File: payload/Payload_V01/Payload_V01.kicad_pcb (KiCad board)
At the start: 2 copper layers, 90.2 x 95.9 mm, 36 parts, among them J1 Screw_Terminal_01x02, J2 Screw_Terminal_01x02, J3 Conn_Coaxial, J4 Conn_Coaxial, J5 Conn_Coaxial, U2 AD9838, U4 STM32F407VETx

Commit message: created payload cutout and exported
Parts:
- moved C10 39.0 mm to (187.0, 57.5), turned to 90 degrees
- moved R4 37.9 mm to (186.9, 53.4), turned to 90 degrees
- moved U2 27.2 mm to (154.3, 128.7)
- moved R1 27.0 mm to (183.1, 57.5), turned to 90 degrees
- moved C18 24.3 mm to (170.8, 64.6), turned to 90 degrees
- moved R2 23.0 mm to (164.0, 53.2), turned to 90 degrees
- moved C5 20.7 mm to (175.9, 65.2), turned to 90 degrees
- moved C14 20.6 mm to (164.0, 57.6), turned to 90 degrees
- moved D1 20.1 mm to (178.2, 92.1)
- moved C6 17.6 mm to (179.6, 65.1), turned to 90 degrees
- moved C7 16.2 mm to (159.8, 52.4)
- moved C12 16.2 mm to (159.8, 55.0)
- moved C16 16.2 mm to (159.8, 57.5)
- moved U4 15.7 mm to (134.1, 129.4)
- moved C15 15.6 mm to (179.5, 57.7), turned to 90 degrees
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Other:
- outline, holes or cut-outs redrawn

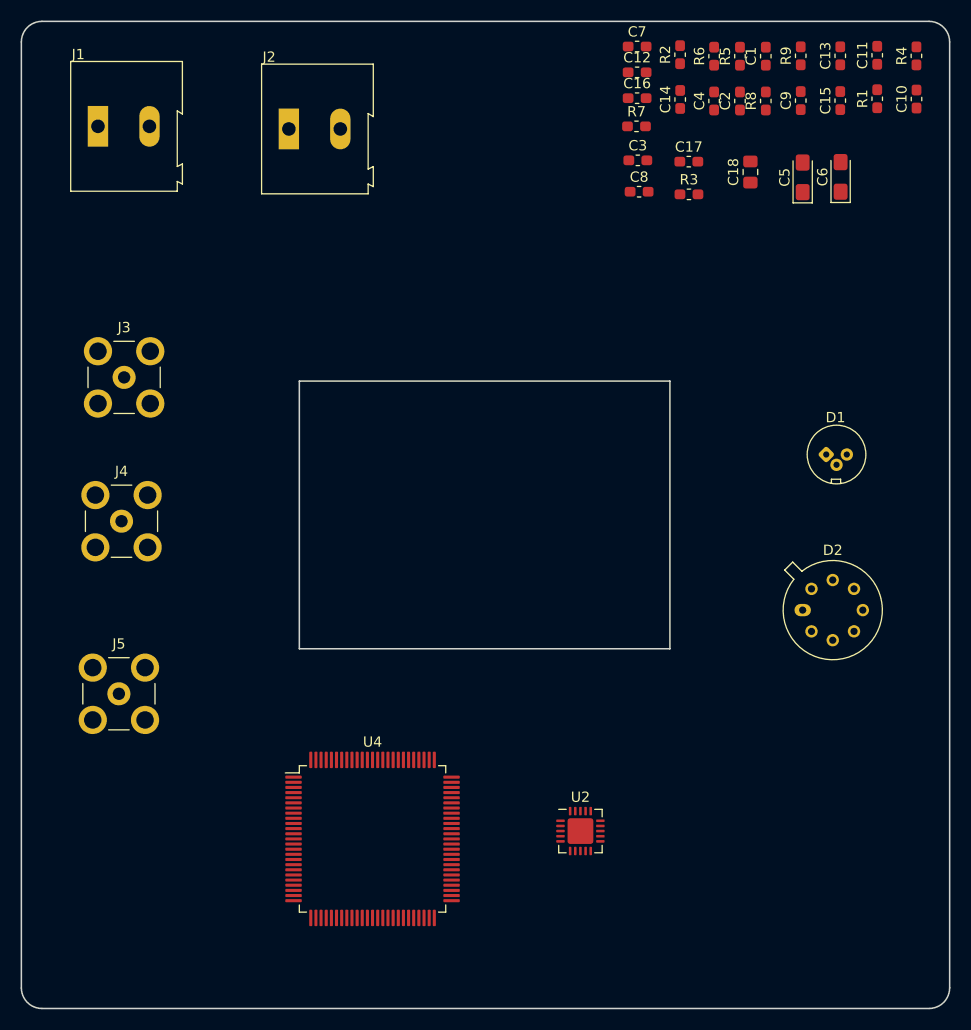
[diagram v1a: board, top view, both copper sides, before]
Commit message: added footprints and 3d models
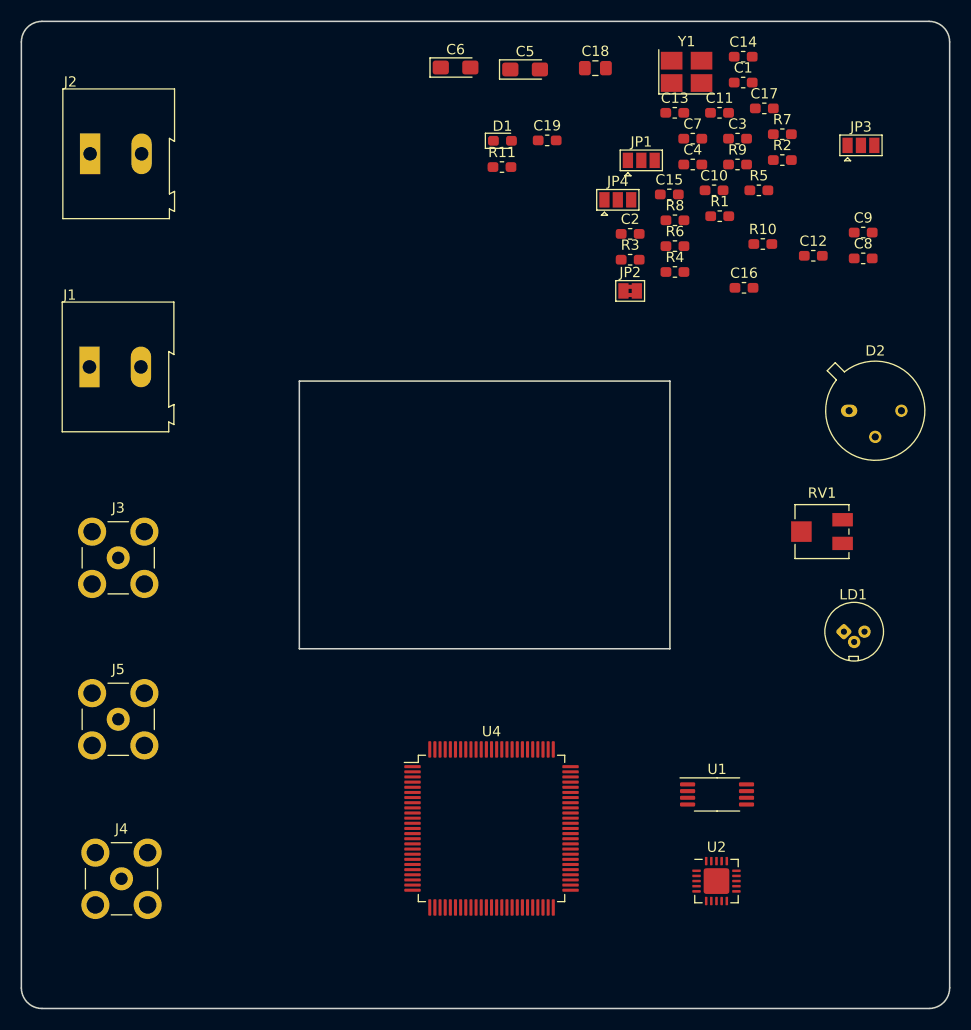
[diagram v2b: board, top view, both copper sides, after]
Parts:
- added C19: C, Resistor_SMD:R_0603_1608Metric_Pad1.05x0.95mm_HandSolder, F.Cu at (151.1, 61.6)
- added JP1: Jumper_3_Open, Jumper:SolderJumper-3_P1.3mm_Open_Pad1.0x1.5mm, F.Cu at (160.2, 63.5)
- added JP2: Jumper, Jumper:SolderJumper-2_P1.3mm_Bridged2Bar_Pad1.0x1.5mm, F.Cu at (159.1, 76.2)
- added JP3: Jumper_3_Open, Jumper:SolderJumper-3_P1.3mm_Open_Pad1.0x1.5mm, F.Cu at (181.6, 62.0)
- added JP4: Jumper_3_Open, Jumper:SolderJumper-3_P1.3mm_Open_Pad1.0x1.5mm, F.Cu at (157.9, 67.3)
- added LD1: DJ532-40, OptoDevice:LaserDiode_TO18-D5.6-3, F.Cu at (179.9, 109.3)
- added R10: 1k, Resistor_SMD:R_0603_1608Metric_Pad1.05x0.95mm_HandSolder, F.Cu at (172.0, 71.6)
- added R11: R_US, Resistor_SMD:R_0603_1608Metric_Pad1.05x0.95mm_HandSolder, F.Cu at (146.7, 64.2)
- added RV1: 10k, Potentiometer_SMD:Potentiometer_Vishay_TS53YJ_Vertical, F.Cu at (177.8, 99.6)
- added U1: REF196, Package_SO:TSSOP-8_4.4x3mm_P0.65mm, F.Cu at (167.6, 125.1)
- added Y1: SG-310SCF, Crystal:Crystal_SMD_SeikoEpson_TSX3225-4Pin_3.2x2.5mm_HandSoldering, F.Cu at (164.6, 54.9)
- D1: footprint OptoDevice:LaserDiode_TO18-D5.6-3 -> Diode_SMD:D_0603_1608Metric_Pad1.05x0.95mm_HandSolder
- D2: footprint Package_TO_SOT_THT:TO-5-8 -> Package_TO_SOT_THT:TO-5-3
- moved D1 43.8 mm to (146.7, 61.6)
- moved C6 38.9 mm to (142.2, 54.5), turned to 0 degrees
- moved J4 34.7 mm to (109.7, 133.3)
- moved R4 31.5 mm to (163.5, 74.3), turned to 0 degrees
- moved C5 28.9 mm to (148.9, 54.7), turned to 0 degrees
- moved C12 24.7 mm to (176.9, 72.8)
- moved J1 23.4 mm to (106.6, 83.6)
- moved C8 22.7 mm to (181.8, 73.0)
- moved C10 21.6 mm to (167.3, 66.4), turned to 0 degrees
- moved C16 21.1 mm to (170.2, 75.9)
- moved D2 19.9 mm to (180.4, 87.8)
- moved J2 19.5 mm to (106.7, 62.9)
- moved R1 19.1 mm to (167.8, 68.9), turned to 0 degrees
- moved C15 18.9 mm to (162.9, 66.8), turned to 0 degrees
- moved R6 18.8 mm to (163.5, 71.8), turned to 0 degrees
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
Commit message: added driver footprint and model
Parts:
- added U3: MLD203CLN, Payload_V01:MLD203CLN, F.Cu at (133.7, 72.8)

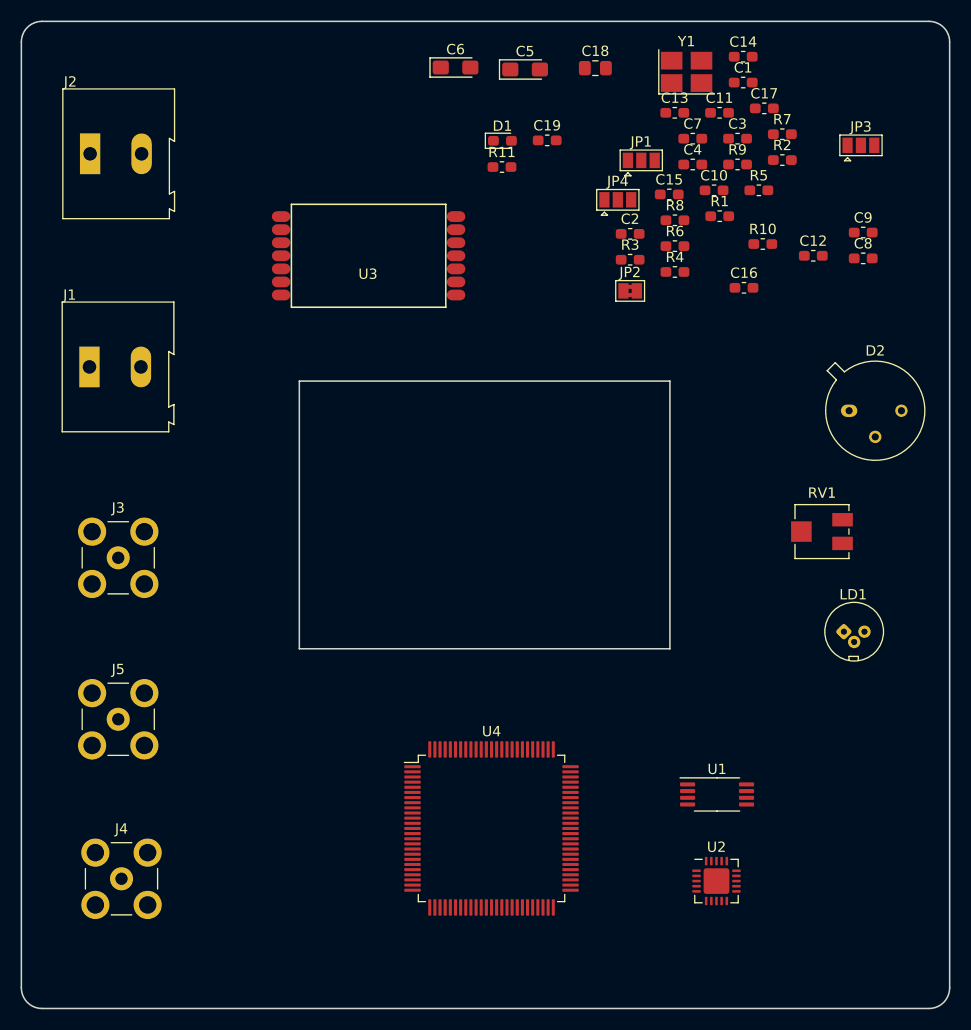
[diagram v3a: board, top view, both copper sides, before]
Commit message: fixed op amp footprint
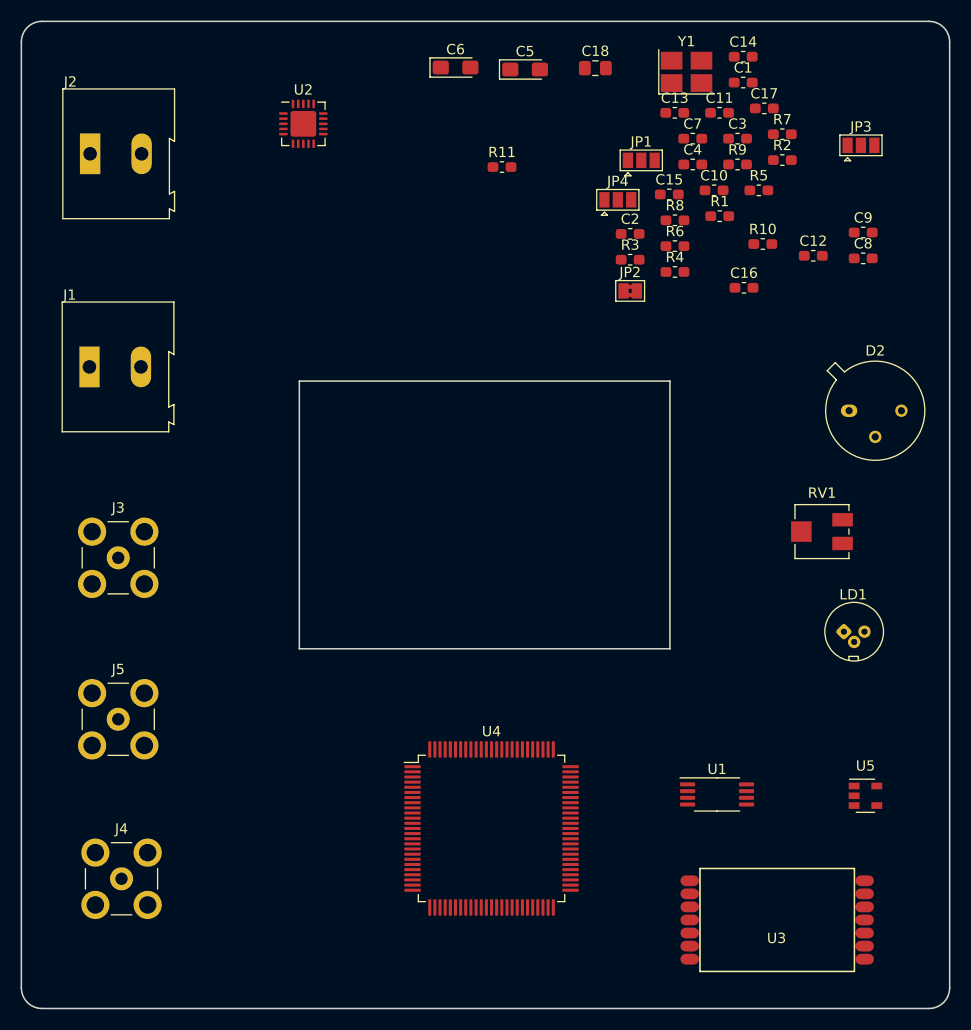
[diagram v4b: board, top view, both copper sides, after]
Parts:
- removed C19: C, Resistor_SMD:R_0603_1608Metric_Pad1.05x0.95mm_HandSolder
- removed D1: D, Diode_SMD:D_0603_1608Metric_Pad1.05x0.95mm_HandSolder
- added U5: LM321, Package_TO_SOT_SMD:SOT-23-5, F.Cu at (182.0, 125.2)
- moved U2 83.8 mm to (127.4, 60.0)
- moved U3 75.7 mm to (173.4, 137.3)
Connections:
- C3 pad 1: VDDA -> +3V3
- C4 pad 1: VDD -> +3V3
- C5 pad 1: VDDA -> +3V3
- C6 pad 1: VDD -> +3V3
- D2 pad 2: Net-(D2-Pad2) -> GND
- J1 pad 1: VDDA -> +3V3
- J2 pad 1: VDD -> +3V3
- JP1 pad 3: VDD -> +3V3
- JP3 pad 1: VDD -> +3V3
- JP4 pad 1: VDDA -> +3V3
- R11 pad 2: Net-(R11-Pad2) -> Net-(D2-Pad1)

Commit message: did some wiring
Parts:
- moved U5 92.7 mm to (122.8, 53.9), turned to 90 degrees
- moved C9 68.9 mm to (112.9, 73.7), turned to 90 degrees
- moved R10 68.9 mm to (186.8, 139.0), turned to 90 degrees
- moved U1 67.4 mm to (153.0, 59.2)
- moved C10 49.1 mm to (118.2, 69.2), turned to 90 degrees
- moved R1 48.0 mm to (121.2, 80.5), turned to 180 degrees
- moved RV1 46.6 mm to (156.5, 141.1), turned to 90 degrees
- moved R2 45.5 mm to (130.4, 76.8), turned to 180 degrees
- moved C15 44.4 mm to (118.6, 64.3)
- moved C11 43.3 mm to (124.9, 64.5)
- moved R4 42.3 mm to (121.2, 75.4), turned to 180 degrees
- moved C12 38.2 mm to (139.8, 63.8), turned to 180 degrees
- moved JP2 37.2 mm to (122.6, 69.2), turned to 90 degrees
- moved JP3 36.5 mm to (146.0, 53.7)
- moved C14 36.1 mm to (135.7, 64.5)
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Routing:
- net +3V3: track 0.00 -> 135.0 mm, vias 0 -> 3
- net Net-(C17-Pad1): track 0.00 -> 102.0 mm, vias 0 -> 2
- net Net-(C18-Pad1): track 0.00 -> 96.2 mm, vias 0 -> 4
- net Net-(D2-Pad1): track 0.00 -> 75.5 mm, vias 0 -> 2
- net GND: track 0.00 -> 47.1 mm, vias 0 -> 4
- net Net-(C7-Pad1): track 0.00 -> 45.8 mm
- net Net-(J3-Pad1): track 0.00 -> 44.5 mm
- net /rf_generator/DVDD_1: track 0.00 -> 37.6 mm
- net Net-(LD1-Pad2): track 0.00 -> 32.6 mm
- net Net-(LD1-Pad3): track 0.00 -> 29.7 mm
- net Net-(C13-Pad2): track 0.00 -> 25.9 mm, vias 0 -> 2
- net Net-(C12-Pad2): track 0.00 -> 23.2 mm
- net Net-(C10-Pad1): track 0.00 -> 18.2 mm
- net Net-(C15-Pad2): track 0.00 -> 17.6 mm, vias 0 -> 2
- net Net-(C16-Pad1): track 0.00 -> 17.5 mm
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- added copper zone on F.Cu, net GND

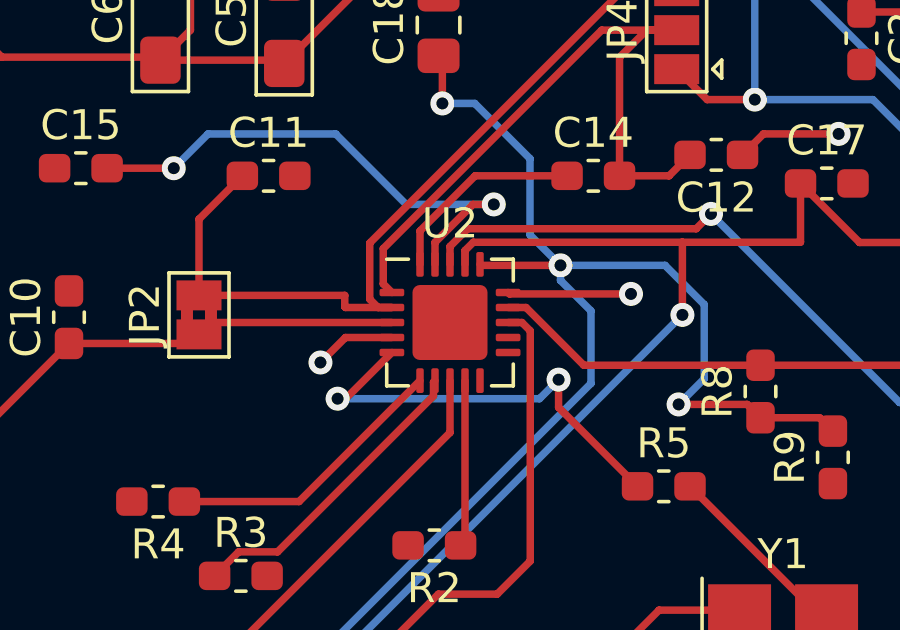
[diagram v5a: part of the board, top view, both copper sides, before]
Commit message: tested labels to get microcontroller working
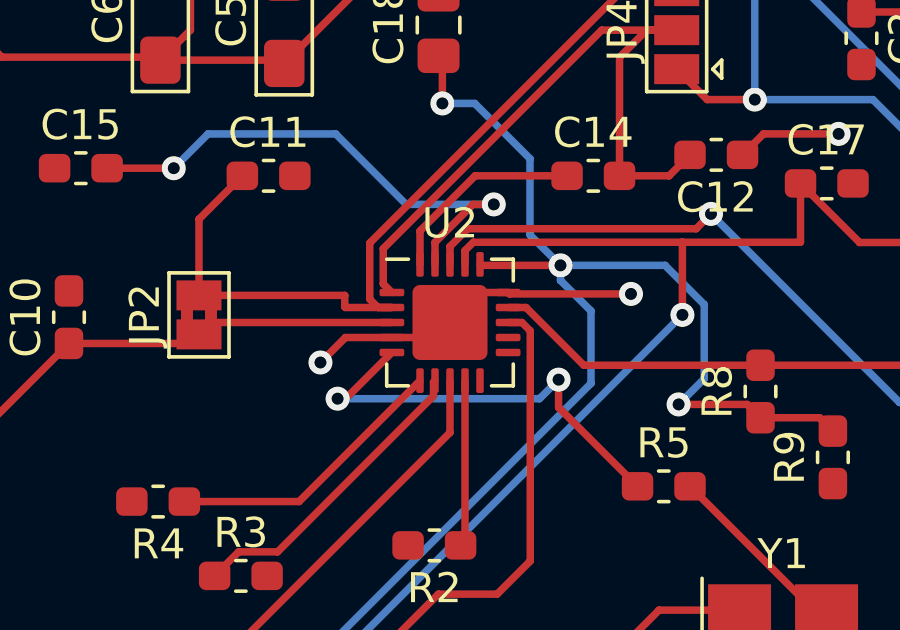
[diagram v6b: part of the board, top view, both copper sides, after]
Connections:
- net /rf_generator/3.3V_BF renamed /rf_generator/3,3V_BF
- net /rf_generator/DVDD_1 renamed /rf_generator/DVDD1
- U2 pad 11: /rf_generator/SCLK -> /Microcontroller/SCLK
- U2 pad 21: (no net) -> GND
- U4 pad 2: Net-(U4-Pad2) -> /Microcontroller/SCLK
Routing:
- net GND: track 47.1 -> 51.6 mm

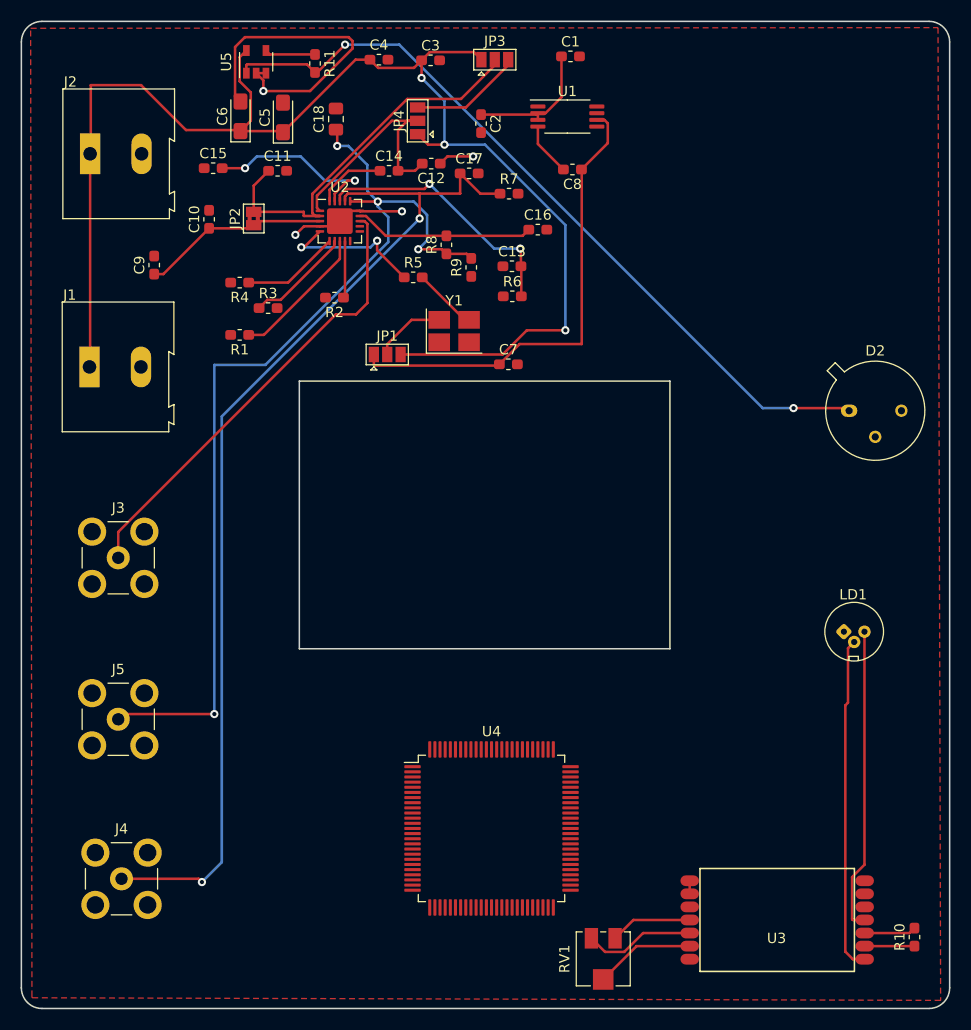
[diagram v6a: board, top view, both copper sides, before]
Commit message: fixed laser driver
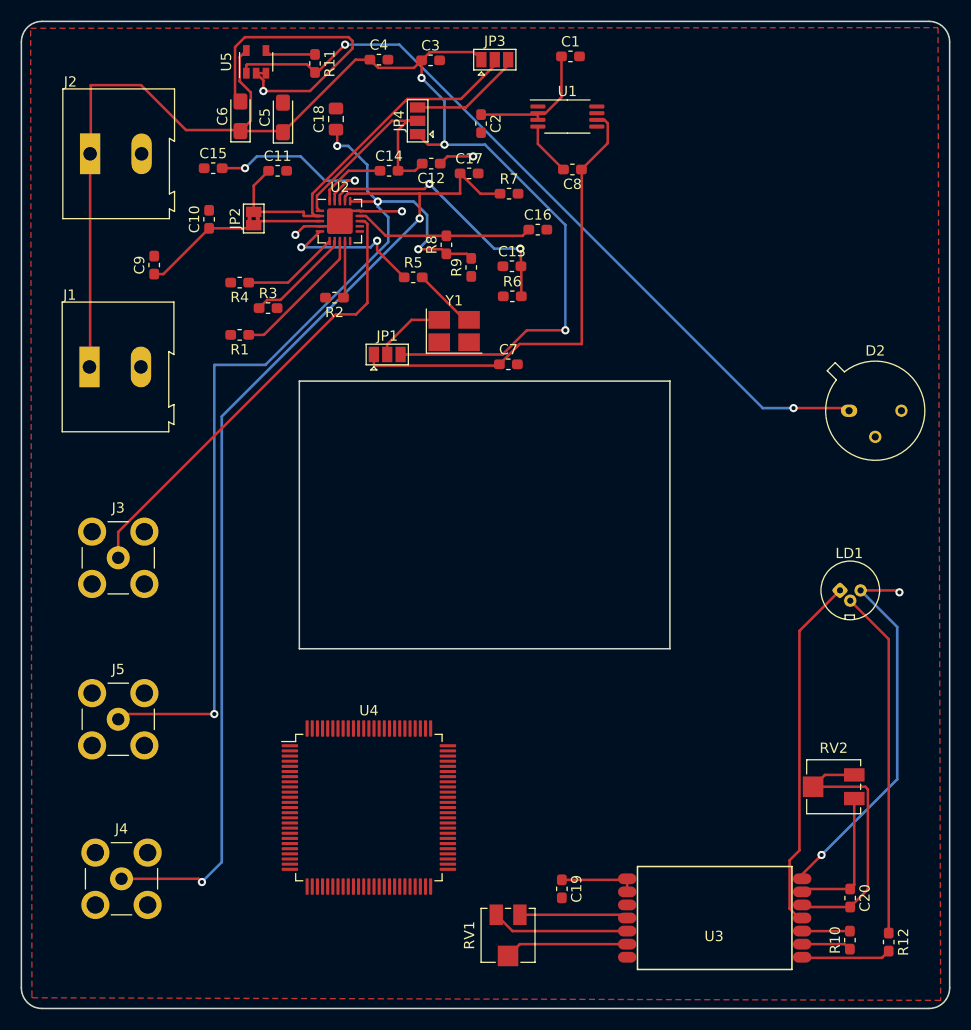
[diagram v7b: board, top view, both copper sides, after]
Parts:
- added C19: C, Capacitor_SMD:C_0603_1608Metric_Pad1.05x0.95mm_HandSolder, F.Cu at (152.5, 134.3)
- added C20: C, Capacitor_SMD:C_0603_1608Metric_Pad1.05x0.95mm_HandSolder, F.Cu at (180.5, 135.2)
- added R12: R_US, Resistor_SMD:R_0603_1608Metric_Pad1.05x0.95mm_HandSolder, F.Cu at (184.3, 139.4)
- added RV2: 10k, Potentiometer_SMD:Potentiometer_Vishay_TS53YJ_Vertical, F.Cu at (178.9, 124.3)
- LD1: value DJ532-40 -> Laserdiode_N_TYPE
- U3: value MLD203CLN -> MLD203P1
- moved U4 12.1 mm to (133.8, 126.4)
- moved RV1 9.52 mm to (147.3, 138.8)
- moved R10 6.28 mm to (180.5, 139.2)
- moved U3 6.07 mm to (167.3, 137.1)
- moved LD1 4.03 mm to (179.5, 105.3)
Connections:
- net /rf_generator/3,3V_BF renamed /rf_generator/3.3V_BF
- net Net-(R11-Pad1) renamed /Photodiode/PD_OUT
- LD1 pad 1: (no net) -> Net-(LD1-Pad1)
- U2 pad 11: /Microcontroller/SCLK -> /rf_generator/SCLK
- U2 pad 21: GND -> (no net)
- U3 pad 11: Net-(LD1-Pad3) -> Net-(LD1-Pad1)
- U3 pad 14: Net-(LD1-Pad2) -> Net-(R12-Pad2)
- U3 pad 8: Net-(U3-Pad8) -> Net-(LD1-Pad3)
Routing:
- net Net-(LD1-Pad1): track 0.00 -> 34.5 mm
- net Net-(C20-Pad2): track 0.00 -> 26.8 mm
- net Net-(C20-Pad1): track 0.00 -> 13.7 mm
- net Net-(R12-Pad2): track 0.00 -> 8.70 mm
- net Net-(LD1-Pad3): track 29.7 -> 37.2 mm, vias 0 -> 2
- net +5V: track 1.27 -> 7.66 mm
- net Net-(RV1-Pad3): track 7.98 -> 10.6 mm
- net Net-(RV1-Pad1): track 10.9 -> 13.4 mm
- net Net-(RV1-Pad2): track 9.74 -> 12.0 mm
- net Net-(LD1-Pad2): track 32.6 -> 33.8 mm
